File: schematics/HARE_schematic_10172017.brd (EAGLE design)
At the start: 105.1 x 80 mm, 91 parts, among them IC1 NE5532N, IC2 NE5532N, IC3 FT232RL, IC4 NE5532N, IC5 7805DT, J2 STEREOSW, J3 STEREOSW, Q1 16 MHz, SW1 3PDTBLUE, SW2 Reset Button, U1 ATMEGA328P-PU, X2 USB-B-H

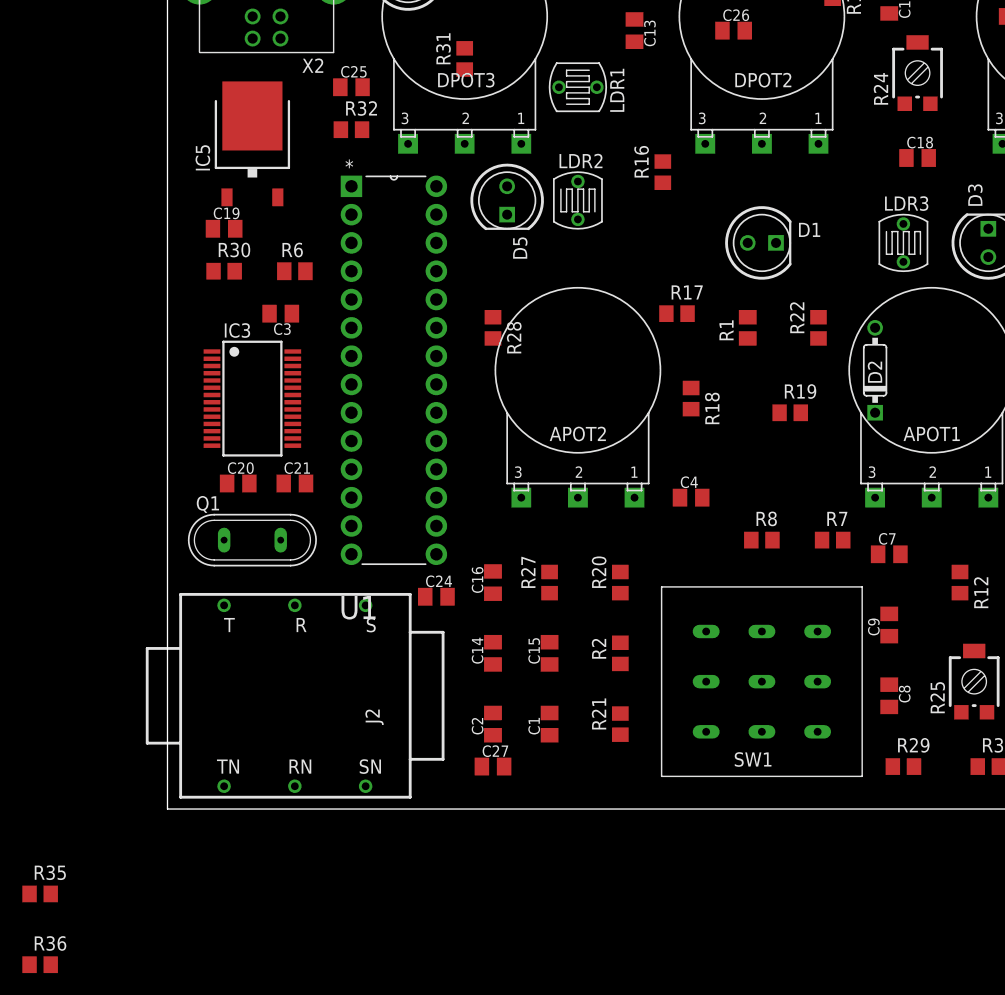
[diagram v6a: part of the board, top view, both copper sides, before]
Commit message: Resolved errors and most warnings in ERC
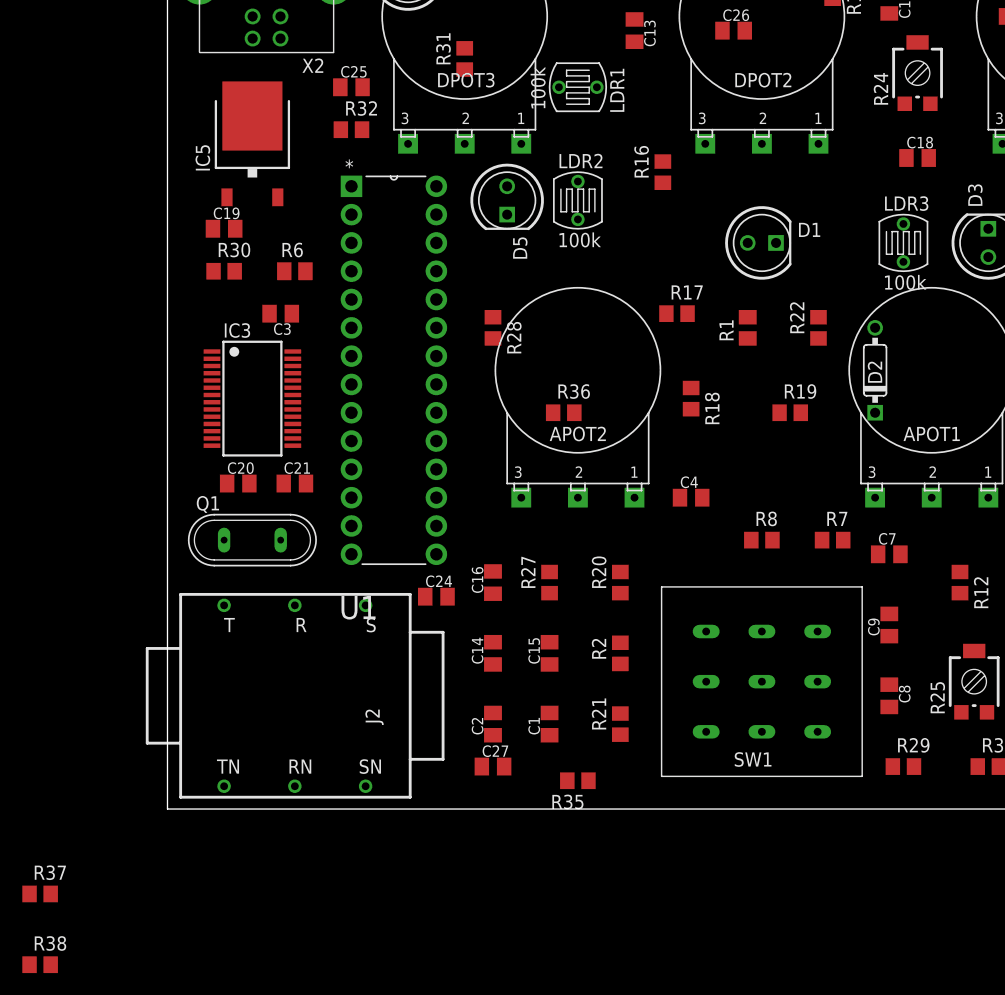
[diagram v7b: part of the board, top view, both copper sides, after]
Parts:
- added R37, R38: 1k, resistor:R0805
- APOT1, DPOT1, DPOT2, DPOT3, LDR1, LDR2, LDR3: value (none) -> 100k
- APOT2: value (none) -> 250k
- J1: value (none) -> 9V
- R35, R36: value 1k -> 10k
- moved R36 68.3 mm to (35.6, 35.6)
- moved R35 49.3 mm to (36.8, 2.54), turned to 180 degrees
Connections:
- removed net N$26: C10.2
- removed net N$48: APOT1.1
- removed net N$65: IC3.13
- removed net N$66: IC3.22
- removed net N$68: IC3.4
- new net N$24: IC3.10, IC3.2, IC3.6, IC3.9, R37.2
- new net N$28: IC3.27, R38.2
- net 5V: now also U1.21
- net CBUS1: now also IC3.22
- net CBUS2: now also IC3.13
- net DRY: now also APOT1.1
- net GND: now also R37.1, R38.1
- net VCCIO: now also IC3.4
- net VCF_IN: now also C10.2
